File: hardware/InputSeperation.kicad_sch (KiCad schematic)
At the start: 10 parts, among them U13 LM397

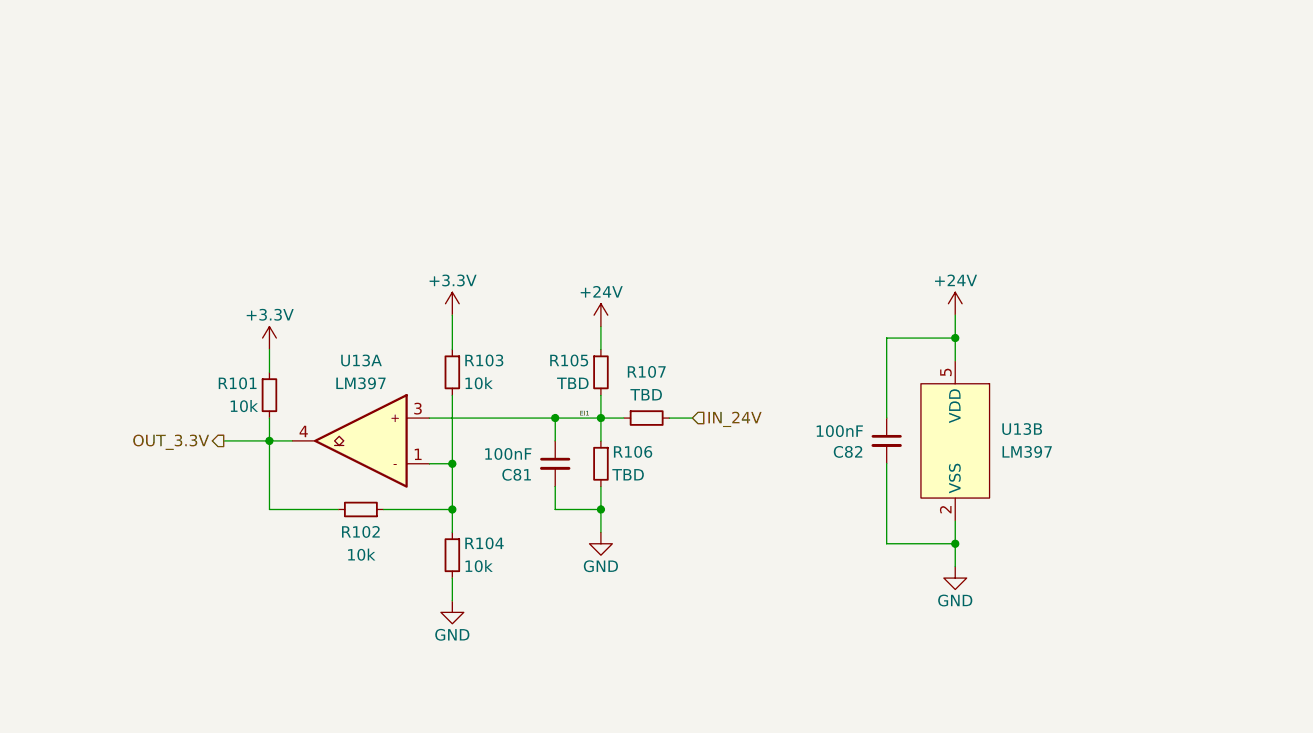
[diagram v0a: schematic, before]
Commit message: the connectors wil stay and wont be changed further
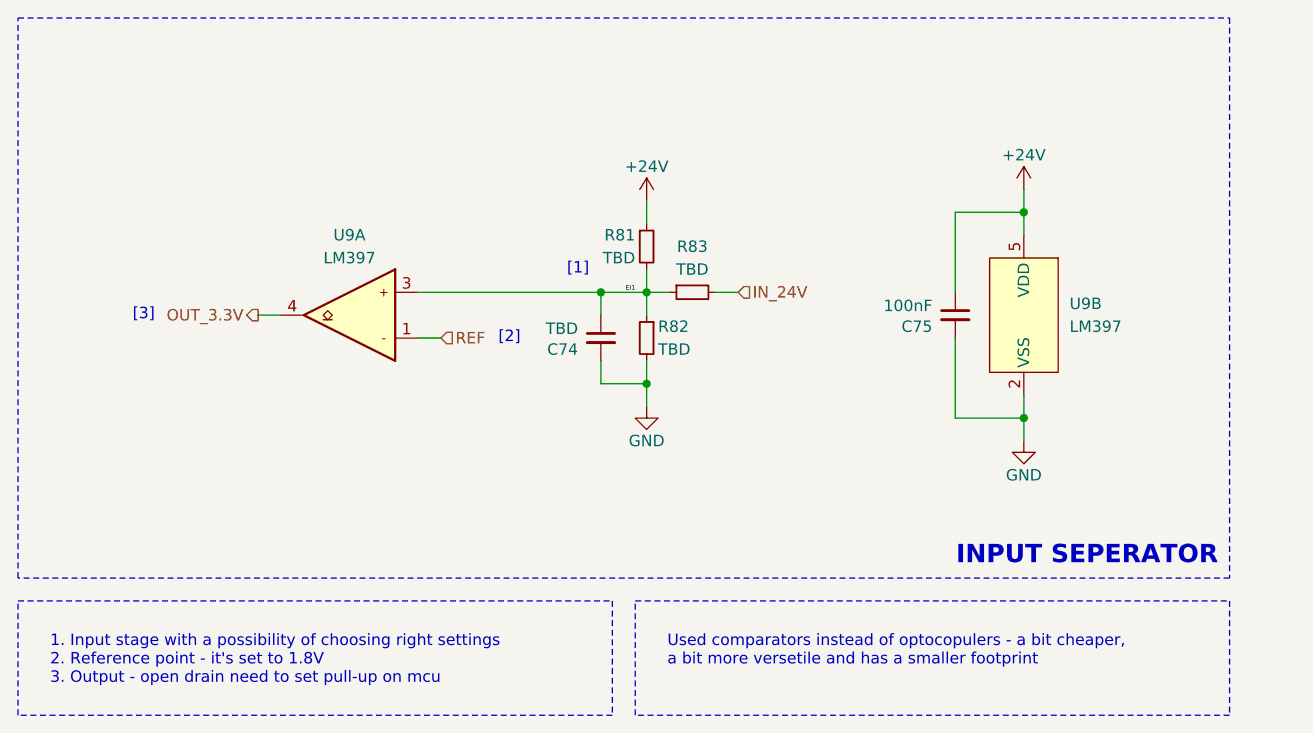
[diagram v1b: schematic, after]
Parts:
- removed R101, R102, R103, R104: 10k, Resistor_SMD:R_0603_1608Metric, symbol Device:R_Small
- C74: renamed from C81; value 100nF -> TBD
- renumbered C82 to C75, R105 to R81, R106 to R82, R107 to R83, U13 to U9
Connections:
- net REF: now reaches U9.1
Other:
- note added: "INPUT SEPERATOR"
- note added: "[1]"
- note added: "[2]"
- note added: "[3]"
- moved on the sheet: C74, C75, R81, R82, R83, U9A, U9B

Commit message: layotu done, some more routing done
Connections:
- net EI1 renamed IN+
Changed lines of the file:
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@@
 		)
 	)
-	(label "EI1"
+	(label "IN+"
 		(at 151.13 86.36 180)
 		(fields_autoplaced yes)

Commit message: sync, layout done, now its time for the routing
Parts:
- removed R81: TBD, Resistor_SMD:R_0603_1608Metric, symbol Device:R_Small
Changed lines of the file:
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@@
-	(wire
-		(pts
-			(xy 152.4 76.2) (xy 152.4 78.74)
-		)
-		(stroke
-			(width 0)
-			(type default)
-		)
-	)
 	(wire
 		(pts
@@
 		(pts
 			(xy 186.69 77.47) (xy 186.69 86.36)
-		)
-		(stroke
-			(width 0)
-			(type default)
-		)
-	)
-	(wire
-		(pts
-			(xy 152.4 83.82) (xy 152.4 86.36)
 		)
 		(stroke
@@
 	)
 	(symbol
-		(lib_name "VDD_2")
-		(lib_id "power:VDD")
-		(at 152.4 76.2 0)
-		(unit 1)
-		(exclude_from_sim no)
-		(in_bom yes)
-		(on_board yes)
-		(dnp no)
-		(property "Reference" "#PWR0142"
-			(at 152.4 80.01 0)
-			(effects
-				(font
-					(size 1.27 1.27)
-				)
-				(hide yes)
-			)
-		)
-		(property "Value" "+24V"
-			(at 152.4 72.39 0)
-			(effects
-				(font
-					(size 1.27 1.27)
-				)
-			)
-		)
-		(property "Footprint" ""
-			(at 152.4 76.2 0)
-			(effects
-				(font
-					(size 1.27 1.27)
-				)
-				(hide yes)
-			)
-		)
-		(property "Datasheet" ""
-			(at 152.4 76.2 0)
-			(effects
-				(font
-					(size 1.27 1.27)
-				)
-				(hide yes)
-			)
-		)
-		(property "Description" ""
-			(at 152.4 76.2 0)
-			(effects
-				(font
-					(size 1.27 1.27)
-				)
-				(hide yes)
-			)
-		)
-		(pin "1"
-		)
-		(instances
-			(project "PUTM_EV_AMS_MASTER_2025"
-				(path "/b456cffc-d9d7-4c91-91f2-36ec9a65dd1b/c7d64097-44d3-49d9-9a80-8f2f4ff55e04/50824e4c-3a23-46ed-a6a0-b956059fc001"
-					(reference "#PWR0142")
-					(unit 1)
-				)
-				(path "/b456cffc-d9d7-4c91-91f2-36ec9a65dd1b/c7d64097-44d3-49d9-9a80-8f2f4ff55e04/850c2180-a634-437d-8598-d7516be18fb3"
-					(reference "#PWR032")
-					(unit 1)
-				)
-				(path "/b456cffc-d9d7-4c91-91f2-36ec9a65dd1b/c7d64097-44d3-49d9-9a80-8f2f4ff55e04/91f3f49c-791c-4c8e-878a-f1a86cae1b35"
-					(reference "#PWR071")
-					(unit 1)
-				)
-				(path "/b456cffc-d9d7-4c91-91f2-36ec9a65dd1b/c7d64097-44d3-49d9-9a80-8f2f4ff55e04/af25626c-6516-4a84-af7c-6fa2b3e0256c"
-					(reference "#PWR0164")
-					(unit 1)
-				)
-				(path "/b456cffc-d9d7-4c91-91f2-36ec9a65dd1b/c7d64097-44d3-49d9-9a80-8f2f4ff55e04/ca5dc7a3-a7a4-462d-9283-6de561582cc8"
-					(reference "#PWR0124")
-					(unit 1)
-				)
-			)
-		)
-	)
-	(symbol
 		(lib_id "Device:R_Small")
 		(at 152.4 91.44 0)
@@
 					(unit 1)
 				)
-			)
-		)
-	)
-	(symbol
-		(lib_id "Device:R_Small")
-		(at 152.4 81.28 0)
-		(unit 1)
-		(exclude_from_sim no)
-		(in_bom yes)
-		(on_board yes)
-		(dnp no)
-		(property "Reference" "R81"
-			(at 151.13 80.01 0)
-			(effects
-				(font
-					(size 1.27 1.27)
-				)
-				(justify right)
-			)
-		)
-		(property "Value" "TBD"
-			(at 151.13 82.55 0)
-			(effects
-				(font
-					(size 1.27 1.27)
-				)
-				(justify right)
-			)
-		)
-		(property "Footprint" "Resistor_SMD:R_0603_1608Metric"
-			(at 152.4 81.28 0)
-			(effects
-				(font
-					(size 1.27 1.27)
-				)
-				(hide yes)
-			)
-		)
-		(property "Datasheet" "~"
-			(at 152.4 81.28 0)
-			(effects
-				(font
-					(size 1.27 1.27)
-				)
-				(hide yes)
-			)
-		)
-		(property "Description" ""
-			(at 152.4 81.28 0)
-			(effects
-				(font
-					(size 1.27 1.27)
-				)
-				(hide yes)
-			)
-		)
-		(property "Manufacturer_Name" "--"
-			(at 152.4 81.28 0)
-			(effects
-				(font
-					(size 1.27 1.27)
-				)
-				(hide yes)
-			)
-		)
-		(property "Manufacturer_Part_Number" "--"
-			(at 152.4 81.28 0)
-			(effects
-				(font
-					(size 1.27 1.27)
-				)
-				(hide yes)
-			)
-		)
-		(property "Arrow Part Number" ""
-			(at 152.4 81.28 0)
-			(effects
-				(font
-					(size 1.27 1.27)
-				)
-				(hide yes)
-			)
-		)
-		(property "Arrow Price/Stock" ""
-			(at 152.4 81.28 0)
-			(effects
-				(font
-					(size 1.27 1.27)
-				)
-				(hide yes)
-			)
-		)
-		(pin "1"
-		)
-		(pin "2"
-		)
-		(instances
-			(project "PUTM_EV_AMS_MASTER_2025"
-				(path "/b456cffc-d9d7-4c91-91f2-36ec9a65dd1b/c7d64097-44d3-49d9-9a80-8f2f4ff55e04/50824e4c-3a23-46ed-a6a0-b956059fc001"
-					(reference "R81")
-					(unit 1)
-				)
-				(path "/b456cffc-d9d7-4c91-91f2-36ec9a65dd1b/c7d64097-44d3-49d9-9a80-8f2f4ff55e04/850c2180-a634-437d-8598-d7516be18fb3"
-					(reference "R33")
-					(unit 1)
-				)
-				(path "/b456cffc-d9d7-4c91-91f2-36ec9a65dd1b/c7d64097-44d3-49d9-9a80-8f2f4ff55e04/91f3f49c-791c-4c8e-878a-f1a86cae1b35"
-					(reference "R43")
-					(unit 1)
-				)
-				(path "/b456cffc-d9d7-4c91-91f2-36ec9a65dd1b/c7d64097-44d3-49d9-9a80-8f2f4ff55e04/af25626c-6516-4a84-af7c-6fa2b3e0256c"
-					(reference "R105")
-					(unit 1)
-				)
-				(path "/b456cffc-d9d7-4c91-91f2-36ec9a65dd1b/c7d64097-44d3-49d9-9a80-8f2f4ff55e04/ca5dc7a3-a7a4-462d-9283-6de561582cc8"
-					(reference "R74")
-					(unit 1)
-				)

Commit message: bom update
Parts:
- C74, C75, R82, R83: Mouser Part Number (none) -> --
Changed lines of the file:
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@@
+			)
+		)
+		(property "Mouser Part Number" "--"
+			(at 186.69 88.9 0)
+			(effects
+				(font
+					(size 1.27 1.27)
+				)
+				(hide yes)
 			)
 		)
@@
 			)
 		)
+		(property "Mouser Part Number" "--"
+			(at 152.4 91.44 0)
+			(effects
+				(font
+					(size 1.27 1.27)
+				)
+				(hide yes)
+			)
+		)
 		(pin "1"
 		)
@@
 			)
 		)
+		(property "Mouser Part Number" "--"
+			(at 157.48 86.36 0)
+			(effects
+				(font
+					(size 1.27 1.27)
+				)
+				(hide yes)
+			)
+		)
 		(pin "1"
 		)
@@
 			(at 147.32 91.44 0)
 			(effects
+				(font
+					(size 1.27 1.27)
+				)
+				(hide yes)
+			)
+		)
+		(property "Mouser Part Number" "--"
+			(at 147.32 91.44 0)
+			(effects
